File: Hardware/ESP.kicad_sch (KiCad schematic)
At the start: 24 parts, among them J2 USB_C_Receptacle_USB2.0_16P, U1 ESP32-C6-MINI-1/U, U2 TPS2115ADRBR, U8 LT1963AEST-3.3#TRPBF

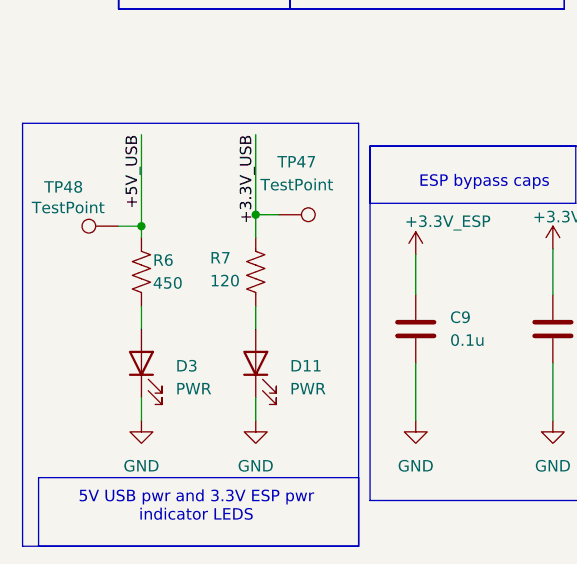
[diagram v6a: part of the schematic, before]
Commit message: added BOM
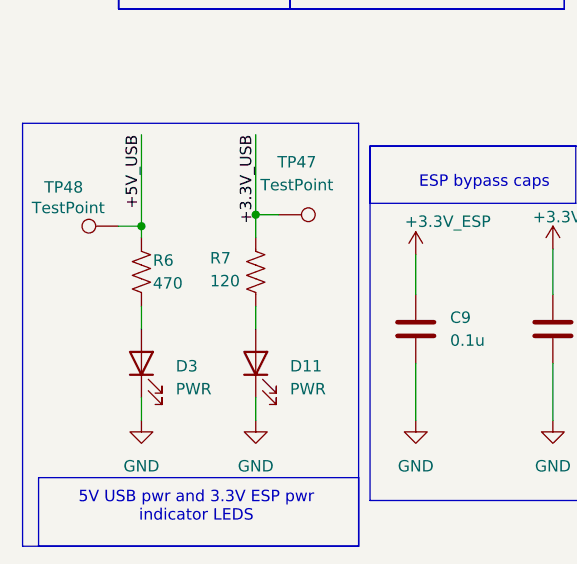
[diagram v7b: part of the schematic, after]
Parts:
- C10, C13: Manufactuerer (none) -> Murata Electronics; P/N MLAST168BB5106MTNA01 -> GRM21BR61H106KE43K
- C11: Manufactuerer (none) -> Murata Electronics; P/N (none) -> GRM21BR61H106KE43K
- C7: Manufactuerer (none) -> Murata Electronics; P/N UMK107B7104KAHT -> GRM21BR61H106KE43K
- D1: Manufactuerer (none) -> Diodes Incorporated
- D11, D3: Manufactuerer (none) -> NATIONSTAR; P/N HSML-C191 -> NCD0603R1
- D2: Manufactuerer (none) -> Littelfuse
- J2: Manufactuerer (none) -> GCT`
- R10, R11: Manufactuerer (none) -> Vishay; P/N (none) -> CRCW06035K10FKEC
- R6: value 450 -> 470; Manufactuerer (none) -> Vishay; P/N (none) -> CRCW1206470RFKEA
- R7: Manufactuerer (none) -> Vishay; P/N (none) -> CRCW0603120RFKEC
- R8: Manufactuerer (none) -> Vishay; P/N (none) -> CRCW06031K00FKEI
- R9: Manufactuerer (none) -> Vishay; P/N (none) -> CRCW060310K0FKEI
- TP47, TP48: now left out of the parts list
- U1: Manufactuerer (none) -> Espressif Systems; P/N (none) -> ESP32-C6-MINI-1U
- U2: Manufactuerer (none) -> Texas Instruments; P/N (none) -> TPS2115ADRBR
- U8: Manufactuerer (none) -> Analog Devices
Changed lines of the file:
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@@
 			)
 		)
-		(property "Datasheet" "~"
+		(property "Datasheet" "https://www.vishay.com/doc?20035"
 			(at 126.365 135.89 0)
 			(effects
@@
 			)
 		)
-		(property "Manufactuerer" ""
+		(property "Manufactuerer" "Vishay "
+			(at 126.365 135.89 0)
+			(effects
+				(font
+					(size 1.27 1.27)
+				)
+				(hide yes)
+			)
+		)
+		(property "P/N" "CRCW06031K00FKEI "
 			(at 126.365 135.89 0)
 			(effects
@@
 			)
 		)
-		(property "Datasheet" ""
+		(property "Datasheet" "https://www.ti.com/lit/gpn/tps2115a"
 			(at 144.78 125.73 0)
 			(effects
@@
 			)
 		)
-		(property "Manufactuerer" ""
+		(property "Manufactuerer" "Texas Instruments "
+			(at 144.78 125.73 0)
+			(effects
+				(font
+					(size 1.27 1.27)
+				)
+				(hide yes)
+			)
+		)
+		(property "P/N" "TPS2115ADRBR"
 			(at 144.78 125.73 0)
 			(effects
@@
 		(unit 1)
 		(exclude_from_sim no)
-		(in_bom yes)
+		(in_bom no)
 		(on_board yes)
 		(dnp no)
@@
 			)
 		)
-		(property "Value" "450"
+		(property "Value" "470"
 			(at 30.48 161.29 0)
 			(effects
@@
 			)
 		)
-		(property "Datasheet" "~"
+		(property "Datasheet" "https://www.vishay.com/doc?20035"
 			(at 29.21 160.02 0)
 			(effects
@@
 			)
 		)
-		(property "Manufactuerer" ""
+		(property "Manufactuerer" "Vishay "
+			(at 29.21 160.02 0)
+			(effects
+				(font
+					(size 1.27 1.27)
+				)
+				(hide yes)
+			)
+		)
+		(property "P/N" "CRCW1206470RFKEA "
 			(at 29.21 160.02 0)
 			(effects
@@
 			)
 		)
-		(property "Datasheet" "~"
+		(property "Datasheet" "https://www.vishay.com/docs/20035/dcrcwe3.pdf"
 			(at 41.91 160.02 0)
 			(effects
@@
 			)
 		)
-		(property "Manufactuerer" ""
+		(property "Manufactuerer" "Vishay "
+			(at 41.91 160.02 0)
+			(effects
+				(font
+					(size 1.27 1.27)
+				)
+				(hide yes)
+			)
+		)
+		(property "P/N" "CRCW0603120RFKEC "
 			(at 41.91 160.02 0)
 			(effects
@@
 			)
 		)
-		(property "Datasheet" "~"
+		(property "Datasheet" "https://www.vishay.com/docs/20035/dcrcwe3.pdf"
 			(at 173.355 120.65 0)
 			(effects
@@
 			)
 		)
-		(property "Manufactuerer" ""
+		(property "Manufactuerer" "Vishay "
+			(at 173.355 120.65 90)
+			(effects
+				(font
+					(size 1.27 1.27)
+				)
+				(hide yes)
+			)
+		)
+		(property "P/N" "CRCW060310K0FKEI "
 			(at 173.355 120.65 90)
 			(effects
@@
 			)
 		)
-		(property "Datasheet" "~"
+		(property "Datasheet" "https://4donline.ihs.com/images/VipMasterIC/IC/DIOD/DIOD-S-A0011437026/DIOD-S-A0011683586-1.pdf?hkey=CECEF36DEECDED6468708AAF2E19C0C6"
 			(at 62.23 33.02 0)
 			(effects
@@
 			)
 		)
-		(property "Manufactuerer" ""
+		(property "Manufactuerer" "Diodes Incorporated "
 			(at 62.23 33.02 0)
 			(effects
@@
 			)
 		)
-		(property "Manufactuerer" ""
+		(property "Manufactuerer" "GCT`"
 			(at 36.83 48.26 0)
 			(effects
@@
 			)
 		)
-		(property "Manufactuerer" ""
+		(property "Manufactuerer" "Analog Devices "
 			(at 124.46 35.56 0)
 			(effects
@@
 			)
 		)
-		(property "Datasheet" "http://www.littelfuse.com/~/media/files/littelfuse/technical%20resources/documents/data%20sheets/sp05xxba.pdf"
+		(property "Datasheet" "https://www.littelfuse.com/assetdocs/tvs-diode-array-spasp050xba-lead-free-green-datasheet?assetguid=15A03DE1-F0C6-457A-95F1-55D449FDD756"
 			(at 125.095 79.375 0)
 			(effects
@@
 			)
 		)
-		(property "Manufactuerer" ""
+		(property "Manufactuerer" "Littelfuse "
 			(at 121.92 82.55 0)
 			(effects
@@
 			)
 		)
-		(property "Datasheet" "https://www.espressif.com/sites/default/files/documentation/esp32-c6-mini-1_datasheet_en.pdf"
+		(property "Datasheet" "https://www.mouser.com/datasheet/3/1574/1/esp32-c6-mini-1_datasheet_en.pdf"
 			(at 228.6 24.13 0)
 			(effects
@@
 			)
 		)
-		(property "Manufactuerer" ""
+		(property "Manufactuerer" "Espressif Systems "
+			(at 228.6 24.13 0)
+			(effects
+				(font
+					(size 1.27 1.27)
+				)
+				(hide yes)
+			)
+		)
+		(property "P/N" "ESP32-C6-MINI-1U"
 			(at 228.6 24.13 0)
 			(effects
@@
 			)
 		)
-		(property "Datasheet" "~"
+		(property "Datasheet" "https://www.lcsc.com/datasheet/C84263.pdf"
 			(at 41.91 170.18 0)
 			(effects
@@
 			)
 		)
-		(property "P/N" "HSML-C191"
+		(property "P/N" "NCD0603R1"
 			(at 41.91 170.18 90)
 			(effects
@@
 			)
 		)
-		(property "Manufactuerer" ""
+		(property "Manufactuerer" "NATIONSTAR"
 			(at 41.91 170.18 90)
 			(effects
@@
 			)
 		)
-		(property "Datasheet" "~"
+		(property "Datasheet" "https://www.lcsc.com/datasheet/C84263.pdf"
 			(at 29.21 170.18 0)
 			(effects
@@
 			)
 		)
-		(property "P/N" "HSML-C191"
+		(property "P/N" "NCD0603R1"
 			(at 29.21 170.18 90)
 			(effects
@@
 			)
 		)
-		(property "Manufactuerer" ""
+		(property "Manufactuerer" "NATIONSTAR"
 			(at 29.21 170.18 90)
 			(effects
@@
 			)
 		)
-		(property "Datasheet" "~"
+		(property "Datasheet" "https://www.vishay.com/doc?20035"
 			(at 52.07 105.41 0)
 			(effects
@@
 			)
 		)
-		(property "Manufactuerer" ""
+		(property "Manufactuerer" "Vishay "
+			(at 52.07 105.41 0)
+			(effects
+				(font
+					(size 1.27 1.27)
+				)
+				(hide yes)
+			)
+		)
+		(property "P/N" "CRCW06035K10FKEC "
 			(at 52.07 105.41 0)
 			(effects
@@
 			)
 		)
-		(property "Datasheet" "~"
+		(property "Datasheet" "https://www.mouser.com/datasheet/3/76/1/GRM21BR61H106KE43_01A.pdf"
 			(at 138.43 38.1 0)
 			(effects
@@
 			)
 		)
-		(property "P/N" "MLAST168BB5106MTNA01"
+		(property "P/N" "GRM21BR61H106KE43K"
 			(at 138.43 38.1 0)
 			(effects
@@
 			)
 		)
-		(property "Manufactuerer" ""
+		(property "Manufactuerer" "Murata Electronics "
 			(at 138.43 38.1 0)
 			(effects
@@
 			)
 		)
-		(property "Datasheet" "~"
+		(property "Datasheet" "https://www.mouser.com/datasheet/3/76/1/GRM21BR61H106KE43_01A.pdf"
 			(at 74.93 166.37 0)
 			(effects
@@
 			)
 		)
-		(property "Manufactuerer" ""
+		(property "Manufactuerer" "Murata Electronics "
+			(at 74.93 166.37 0)
+			(effects
+				(font
+					(size 1.27 1.27)
+				)
+				(hide yes)
+			)
+		)
+		(property "P/N" "GRM21BR61H106KE43K"
 			(at 74.93 166.37 0)
 			(effects
@@
 		(unit 1)
 		(exclude_from_sim no)
-		(in_bom yes)
+		(in_bom no)
 		(on_board yes)
 		(dnp no)
@@
 			)
 		)
-		(property "Datasheet" "~"
+		(property "Datasheet" "https://www.mouser.com/datasheet/3/76/1/GRM21BR61H106KE43_01A.pdf"
 			(at 35.56 106.68 0)
 			(effects
@@
 			)
 		)
-		(property "P/N" "MLAST168BB5106MTNA01"
+		(property "P/N" "GRM21BR61H106KE43K"
 			(at 35.56 106.68 0)
 			(effects
@@
 			)
 		)
-		(property "Manufactuerer" ""
+		(property "Manufactuerer" "Murata Electronics "
 			(at 35.56 106.68 0)
 			(effects
@@
 			)
 		)
-		(property "Datasheet" "~"
+		(property "Datasheet" "https://www.vishay.com/doc?20035"
 			(at 62.23 105.41 0)
 			(effects
@@
 			)
 		)
-		(property "Manufactuerer" ""
+		(property "Manufactuerer" "Vishay "
+			(at 62.23 105.41 0)
+			(effects
+				(font
+					(size 1.27 1.27)
+				)
+				(hide yes)
+			)
+		)
+		(property "P/N" "CRCW06035K10FKEC "
 			(at 62.23 105.41 0)
 			(effects
@@
 			)
 		)
-		(property "Datasheet" "~"
+		(property "Datasheet" "https://www.mouser.com/datasheet/3/76/1/GRM21BR61H106KE43_01A.pdf"
 			(at 109.22 38.1 0)
 			(effects
@@
 			)
 		)
-		(property "P/N" "UMK107B7104KAHT "
+		(property "P/N" "GRM21BR61H106KE43K"
 			(at 109.22 38.1 0)
 			(effects
@@
 			)
 		)
-		(property "Manufactuerer" ""
+		(property "Manufactuerer" "Murata Electronics "
 			(at 109.22 38.1 0)
 			(effects

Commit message: updated BOM
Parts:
- added R14: 3.3k, Resistor_SMD:R_0603_1608Metric, symbol Device:R_US
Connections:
- net +3.3V_ESP: now also R14.1
- net BOOT: now also R14.2
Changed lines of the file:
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@@
 	(wire
 		(pts
+			(xy 120.65 182.88) (xy 120.65 186.69)
+		)
+		(stroke
+			(width 0)
+			(type default)
+		)
+	)
+	(wire
+		(pts
 			(xy 107.315 115.57) (xy 107.315 118.745)
 		)
@@
 	(wire
 		(pts
+			(xy 120.65 172.72) (xy 120.65 175.26)
+		)
+		(stroke
+			(width 0)
+			(type default)
+		)
+	)
+	(wire
+		(pts
 			(xy 179.705 120.65) (xy 179.705 115.57)
 		)
@@
 	(wire
 		(pts
+			(xy 114.3 186.69) (xy 120.65 186.69)
+		)
+		(stroke
+			(width 0)
+			(type default)
+		)
+	)
+	(wire
+		(pts
 			(xy 109.22 33.02) (xy 114.3 33.02)
 		)
@@
 		)
 	)
+	(label "BOOT"
+		(at 114.3 186.69 0)
+		(effects
+			(font
+				(size 1.27 1.27)
+			)
+			(justify left bottom)
+		)
+	)
 	(label "+5V_USB"
 		(at 99.06 33.02 0)
@@
 	)
 	(symbol
+		(lib_id "power:+3V3")
+		(at 120.65 172.72 0)
+		(unit 1)
+		(exclude_from_sim no)
+		(in_bom yes)
+		(on_board yes)
+		(dnp no)
+		(property "Reference" "#PWR0152"
+			(at 120.65 176.53 0)
+			(effects
+				(font
+					(size 1.27 1.27)
+				)
+				(hide yes)
+			)
+		)
+		(property "Value" "+3.3V_ESP"
+			(at 123.19 169.164 0)
+			(effects
+				(font
+					(size 1.27 1.27)
+				)
+			)
+		)
+		(property "Footprint" ""
+			(at 120.65 172.72 0)
+			(effects
+				(font
+					(size 1.27 1.27)
+				)
+				(hide yes)
+			)
+		)
+		(property "Datasheet" ""
+			(at 120.65 172.72 0)
+			(effects
+				(font
+					(size 1.27 1.27)
+				)
+				(hide yes)
+			)
+		)
+		(property "Description" "Power symbol creates a global label with name \"+3V3\""
+			(at 120.65 172.72 0)
+			(effects
+				(font
+					(size 1.27 1.27)
+				)
+				(hide yes)
+			)
+		)
+		(pin "1"
+		)
+		(instances
+			(project "BPS-Leader"
+				(path "/fb37da34-e420-4994-8cc1-079e8c0fa48e/dabc680e-023d-4bcf-9356-bacd091b1cc9"
+					(reference "#PWR0152")
+					(unit 1)
+				)
+			)
+		)
+	)
+	(symbol
 		(lib_id "UTSVT_ICs:TPS2115ADRBR")
 		(at 144.78 125.73 0)
@@
 					(unit 1)
 				)
+			)
+		)
+	)
+	(symbol
+		(lib_id "Device:R_US")
+		(at 120.65 179.07 0)
+		(unit 1)
+		(exclude_from_sim no)
+		(in_bom yes)
+		(on_board yes)
+		(dnp no)
+		(fields_autoplaced yes)
+		(property "Reference" "R14"
+			(at 123.19 177.7999 0)
+			(effects
+				(font
+					(size 1.27 1.27)
+				)
+				(justify left)
+			)
+		)
+		(property "Value" "3.3k"
+			(at 123.19 180.3399 0)
+			(effects
+				(font
+					(size 1.27 1.27)
+				)
+				(justify left)
+			)
+		)
+		(property "Footprint" "Resistor_SMD:R_0603_1608Metric"
+			(at 121.666 179.324 90)
+			(effects
+				(font
+					(size 1.27 1.27)
+				)
+				(hide yes)
+			)
+		)
+		(property "Datasheet" "~"
+			(at 120.65 179.07 0)
+			(effects
+				(font
+					(size 1.27 1.27)
+				)
+				(hide yes)
+			)
+		)
+		(property "Description" "Resistor, US symbol"
+			(at 120.65 179.07 0)
+			(effects
+				(font
+					(size 1.27 1.27)
+				)
+				(hide yes)
+			)
+		)
+		(pin "1"
+		)
+		(pin "2"
+		)
+		(instances
+			(project ""
+				(path "/fb37da34-e420-4994-8cc1-079e8c0fa48e/dabc680e-023d-4bcf-9356-bacd091b1cc9"
+					(reference "R14")
+					(unit 1)
+				)
